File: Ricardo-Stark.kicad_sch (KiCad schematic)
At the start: 49 parts, among them J1 RBUS, U1 ESP32-S3, Y1 R940000171

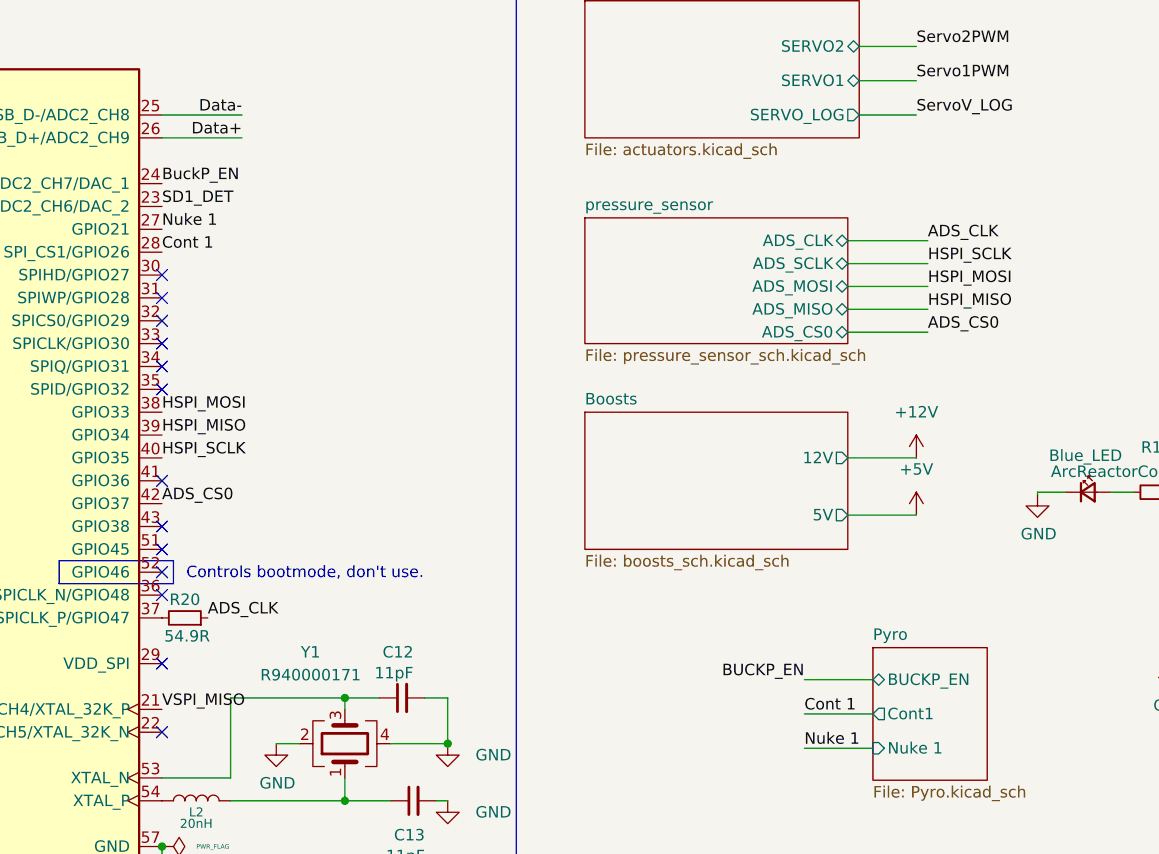
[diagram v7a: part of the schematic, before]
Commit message: Sized sensor resistors and more routing
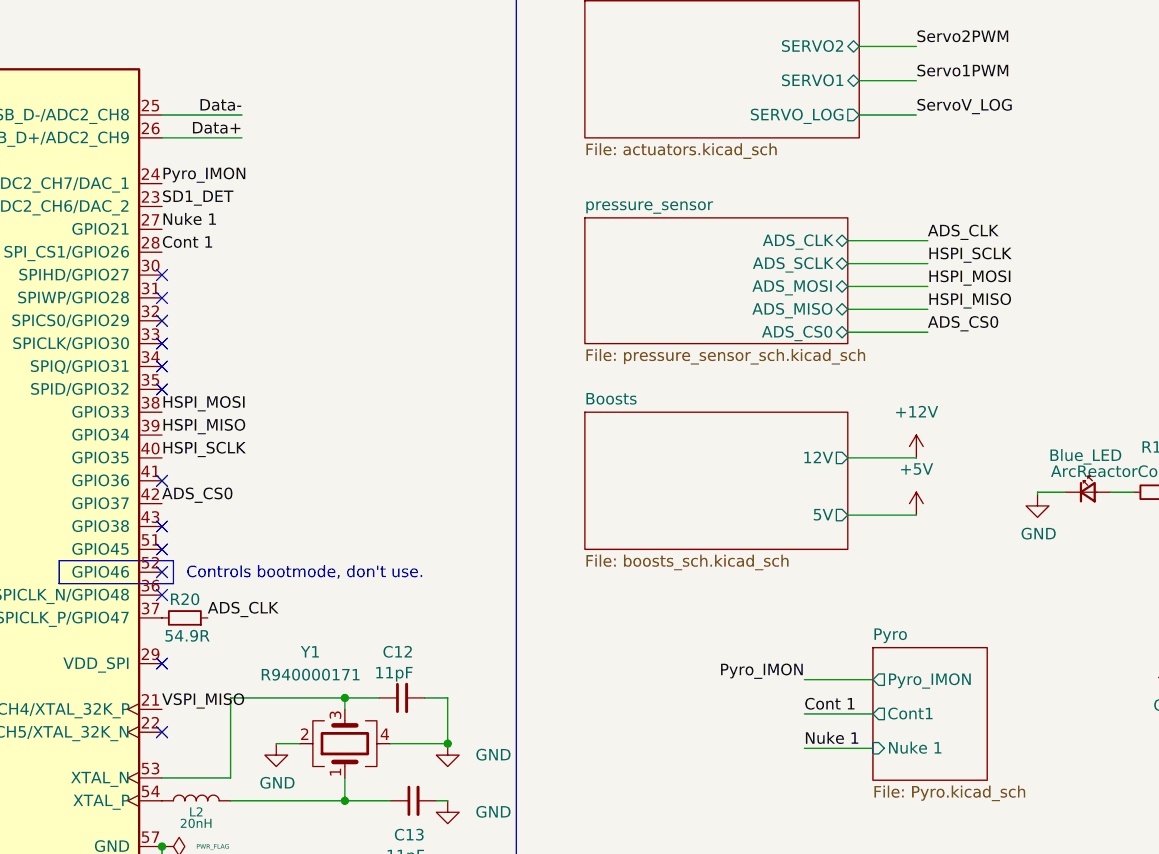
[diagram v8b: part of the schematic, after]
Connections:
- net BuckP_EN renamed Pyro_IMON
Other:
- sheet Pyro ports: added Pyro_IMON; removed BUCKP_EN
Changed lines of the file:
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@@
-    (effects (font (size 1.27 1.27)) (justify left bottom))
-  )
-  (label "BuckP_EN" (at 135.89 69.85 0) (fields_autoplaced)
     (effects (font (size 1.27 1.27)) (justify left bottom))
   )
@@
     (effects (font (size 1.27 1.27)) (justify left bottom))
   )
-  (label "BUCKP_EN" (at 207.264 124.968 180) (fields_autoplaced)
-    (effects (font (size 1.27 1.27)) (justify right bottom))
-  )
   (label "BUCKC_EN" (at 226.06 21.59 180) (fields_autoplaced)
     (effects (font (size 1.27 1.27)) (justify right bottom))
@@
     (effects (font (size 1.27 1.27)) (justify right bottom))
   )
+  (label "Pyro_IMON" (at 135.89 69.85 0) (fields_autoplaced)
+    (effects (font (size 1.27 1.27)) (justify left bottom))
+  )
   (label "CAN+" (at 115.57 185.42 0) (fields_autoplaced)
     (effects (font (size 1.27 1.27)) (justify left bottom))
@@
   )
   (label "BUCKC_EN" (at 69.85 100.33 180) (fields_autoplaced)
+    (effects (font (size 1.27 1.27)) (justify right bottom))
+  )
+  (label "Pyro_IMON" (at 207.264 124.968 180) (fields_autoplaced)
     (effects (font (size 1.27 1.27)) (justify right bottom))
   )
@@
       (effects (font (size 1.27 1.27)) (justify left top))
     )
-    (pin "BUCKP_EN" bidirectional (at 214.884 124.968 180)
-      (effects (font (size 1.27 1.27)) (justify left))
-    )
     (pin "Cont1" output (at 214.884 128.778 180)
       (effects (font (size 1.27 1.27)) (justify left))
@@
       (effects (font (size 1.27 1.27)) (justify left))
     )
+    (pin "Pyro_IMON" output (at 214.884 124.968 180)
+      (effects (font (size 1.27 1.27)) (justify left))
+    )
